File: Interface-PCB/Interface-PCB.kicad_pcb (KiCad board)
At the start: 2 copper layers, 140 x 130 mm, 92 parts, among them IC1 SN74LVC245AN, IC2 TBD62783APG, IC3 TBD62783APG, J1 BARREL_JACK_PAD, J10 LEVEL_SENSOR, J11 TEMPERATURE_SENSOR, J12 TEMPERATURE_SENSOR, J13 CONN_05JST, J14 CONN_05JST, J2 BARREL_JACK_PAD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

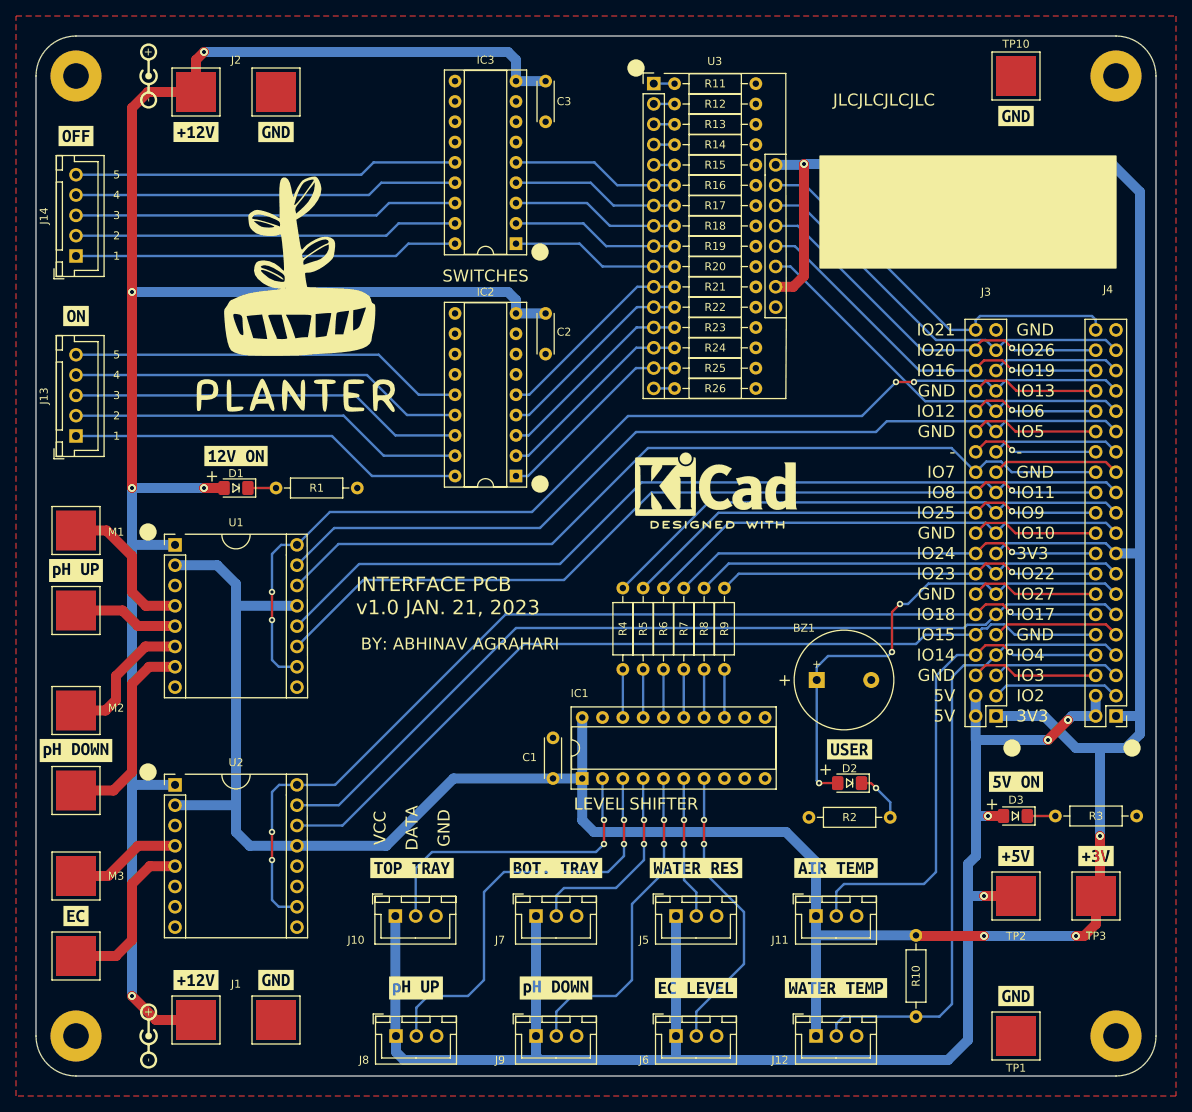
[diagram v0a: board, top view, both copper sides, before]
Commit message: Add 3.3V LDO Regulator and Barrel Jack Connectors
- Add mounted barrel jack connectors for 12V and 5V
- Add 5V to 3.3V LDO breakout board
- Adjust silkscreen
- Export and verify Gerbers
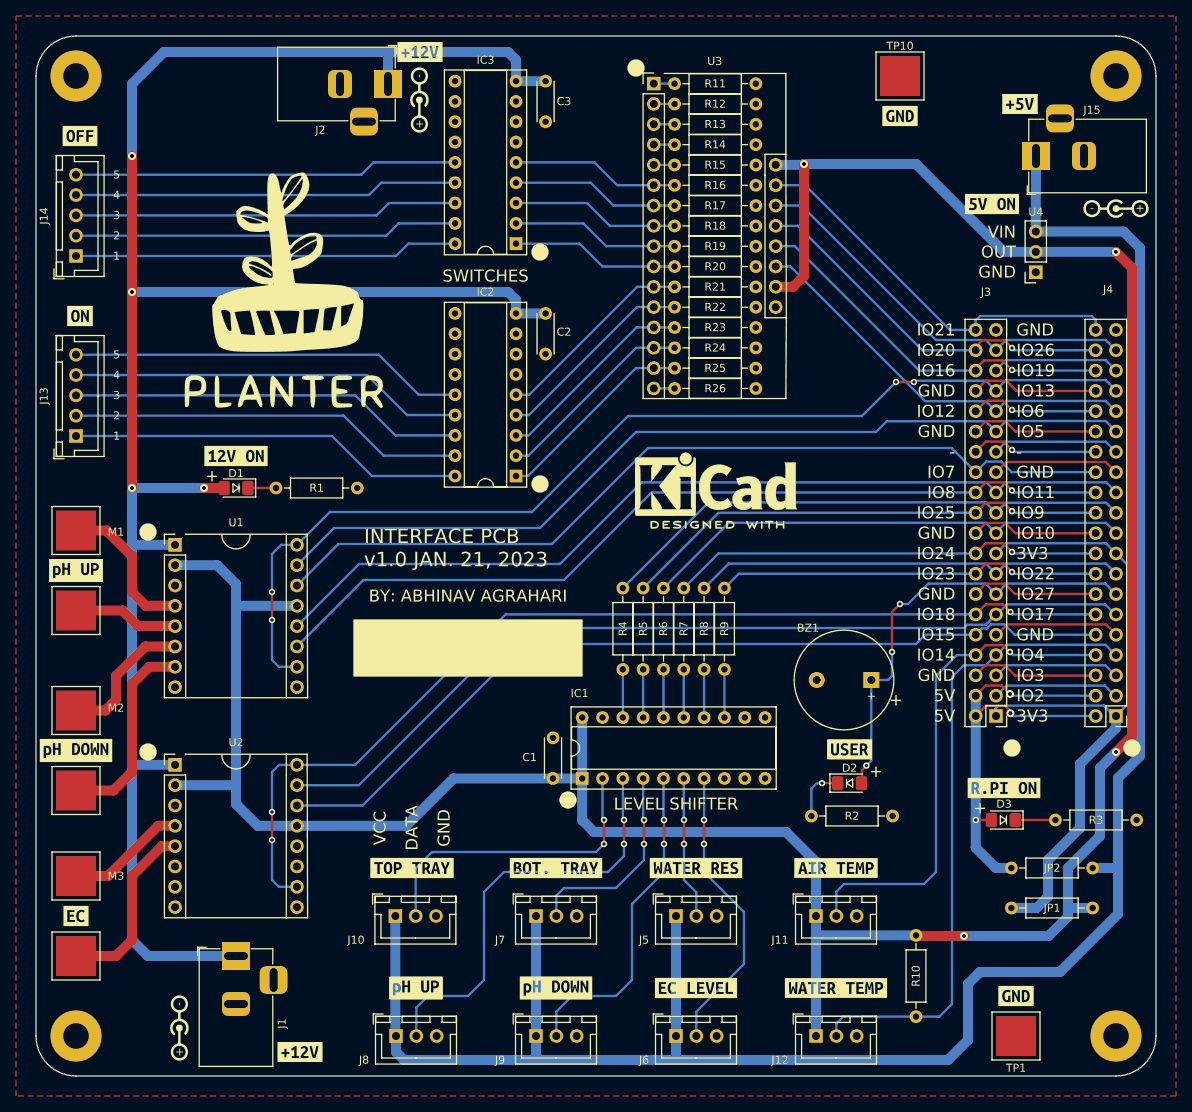
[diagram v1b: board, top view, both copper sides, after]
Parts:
- removed TP2: 5V_PAD, AA_Custom_Components:TestPoint_Pad_5.0x5.0mm
- removed TP3: 3.3V_PAD, AA_Custom_Components:TestPoint_Pad_5.0x5.0mm
- removed kibuzzard-63CB83FB: G***, kibuzzard-63CB83FB
- removed kibuzzard-63CB8656: G***, kibuzzard-63CB8656
- removed the kibuzzard-63CB8663 at (90.0, 153.0)
- removed the kibuzzard-63CB8663 at (90.0, 47.0)
- added J15: Barrel_Jack_THT, AA_Custom_Components:BarrelJack_Horizontal, F.Cu at (185.0, 50.0)
- added JP1: Jumper_2_Open, AA_Custom_Components:R_SS_Axial_DIN0207_L6.3mm_D2.5mm_P10.16mm_Horizontal, F.Cu at (192.1, 144.0)
- added JP2: Jumper_2_Open, AA_Custom_Components:R_SS_Axial_DIN0207_L6.3mm_D2.5mm_P10.16mm_Horizontal, F.Cu at (192.1, 139.0)
- added N4: CENTER_POS, AA_Custom_Components:Polarity_Center_Positive_7.5mm_SilkScreen, F.Cu at (195.0, 56.5)
- added U4: AMS1117-3.3_LDO_Regulator_Breakout, AA_Custom_Components:AMS1117-3.3_LDO_Regulator_Breakout_Board, F.Cu at (185.0, 64.5)
- added kibuzzard-63CDEE5A: G***, kibuzzard-63CDEE5A, F.Cu at (181.0, 129.0)
- added kibuzzard-63CDEE7D: G***, kibuzzard-63CDEE7D, F.Cu at (179.5, 56.0)
- D3: value 5V_ON -> RPI_ON
- J1, J2: value BARREL_JACK_PAD -> Barrel_Jack_THT; footprint AA_Custom_Components:PowerPad_Pair_5.0x5.0mm -> AA_Custom_Components:BarrelJack_Horizontal
- moved kibuzzard-63CB864A 94.0 mm to (183.0, 43.5)
- moved N1 34.1 mm to (108.0, 43.0), turned to -90 degrees
- moved kibuzzard-63CB8737 29.7 mm to (108.0, 37.0)
- moved J2 19.0 mm to (104.0, 41.0)
- moved kibuzzard-63CB8737 15.8 mm to (93.0, 162.0)
- moved TP10 14.5 mm to (168.0, 40.0)
- moved kibuzzard-63CB8663 14.5 mm to (168.0, 45.0)
- moved R2 9.86 mm to (156.9, 132.5), turned to 0 degrees
- moved J1 8.00 mm to (85.0, 150.0), turned to 90 degrees
- moved BZ1 6.82 mm to (164.4, 115.5), turned to 180 degrees
- moved N2 4.12 mm to (78.0, 159.0), turned to -90 degrees
- moved U2 2.50 mm to (85.0, 135.0)
- moved D3 1.58 mm to (180.9, 133.0)
- moved G1 1.58 mm to (91.0, 67.0)
- moved R3 0.50 mm to (187.4, 133.0)
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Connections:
- D3 pad 2: +5V -> +5VD
- J3 pad 1: +3V3 -> +3.3VP
- J3 pad 17: +3V3 -> +3.3VP
- J3 pad 2: +5V -> +5VD
- J3 pad 4: +5V -> +5VD
- J4 pad 1: +3V3 -> +3.3VP
- J4 pad 17: +3V3 -> +3.3VP
- J4 pad 2: +5V -> +5VD
- J4 pad 4: +5V -> +5VD
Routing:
- net +3.3VP: track 0.00 -> 85.7 mm
- net +5V: track 198.8 -> 267.5 mm, vias 4 -> 0
- net +5VD: track 0.00 -> 58.8 mm, vias 0 -> 3
- net +3V3: track 401.1 -> 352.4 mm
- net USER_LED_BUZZER: track 63.3 -> 55.3 mm
- net /EC 2: track 21.1 -> 22.8 mm
- net Net-(D3-Pad1): track 3.51 -> 5.01 mm
- net PWM0: track 130.2 -> 129.1 mm
- net /EC 1: track 13.9 -> 15.0 mm
- net EN_NUT_2: track 113.4 -> 112.3 mm
- net EN_NUT_1: track 110.8 -> 109.8 mm
- net +12V: track 256.1 -> 257.0 mm, vias 5 -> 4
- net Net-(D2-Pad1): track 6.47 -> 7.00 mm
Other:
- board text added: "HIGH SIDE SWITCH"
- board text added: "MOTOR DRIVER"
- board text added: "MUX"
- board text added: "OUT"
- board text added: "VIN"
- board text removed: "IC1"
- board text removed: "IC2"
- board text removed: "IC3"
- board text removed: "U1"
- board text removed: "U2"
- board text removed: "U3"

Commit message: Move Remote Control Barrel Jack
- Move a barrel jack
- Export Gerbers again
- Update images
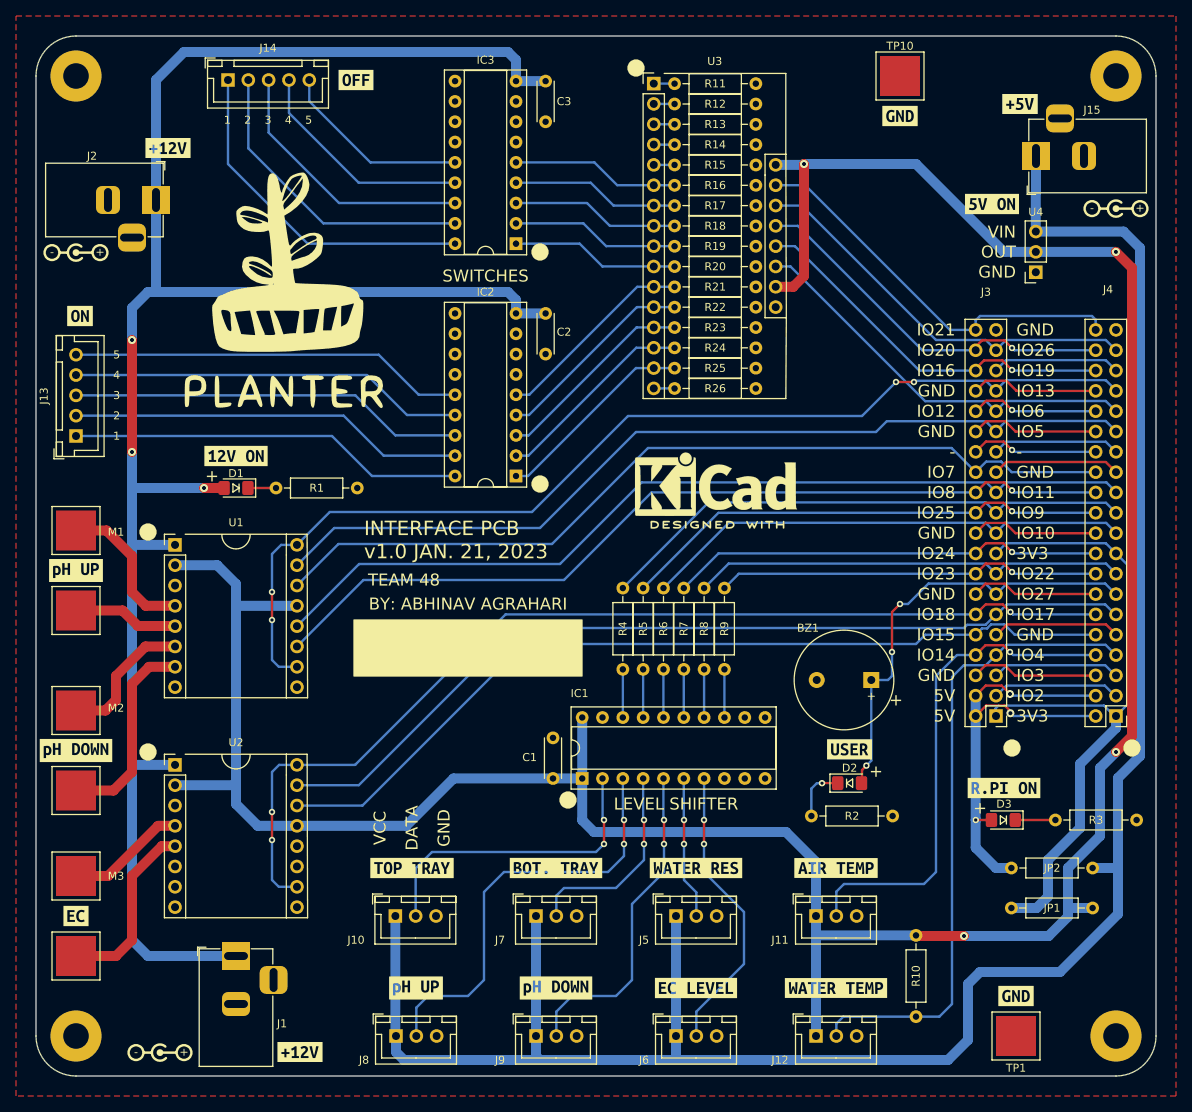
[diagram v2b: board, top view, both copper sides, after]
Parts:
- moved N1 47.0 mm to (65.0, 62.0), turned to 0 degrees
- moved kibuzzard-63CB87CD 35.2 mm to (100.0, 40.5)
- moved kibuzzard-63CB8737 33.7 mm to (76.5, 49.0)
- moved J2 32.4 mm to (75.0, 55.5)
- moved J14 29.1 mm to (84.0, 40.5), turned to 0 degrees
- moved N2 3.91 mm to (75.5, 162.0), turned to 0 degrees
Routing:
- net Net-(IC3-Pad14): track 48.0 -> 24.0 mm
- net Net-(IC3-Pad15): track 48.0 -> 28.5 mm
- net Net-(IC3-Pad16): track 48.0 -> 33.5 mm
- net Net-(IC3-Pad17): track 48.0 -> 38.3 mm
- net +12V: track 257.0 -> 249.1 mm, vias 4 -> 3
- net Net-(IC3-Pad18): track 48.0 -> 43.0 mm
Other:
- board text added: "TEAM 48"
